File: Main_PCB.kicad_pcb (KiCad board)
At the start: 4 copper layers, 161 x 70 mm, 64 parts, among them IC1 TCN75AVUA713-VAO, IC2 24AA64T-I_OT, J1 Conn_Coaxial, J2 Conn_02x03_Odd_Even, J3 USB_C_Receptacle_USB2.0, J4 Conn_01x03_Male, SW1 SW_Push, SW2 SW_Push, U1 LTR-329ALS-01, U2 RFM95W-868S2, U3 1013, U4 STM32L476RGTx, U5 ATECC508A-SSHDA-T, U7 USBLC6-2SC6, Y1 32.768

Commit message: finished pcb
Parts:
- added ?: , logo's:PULU_LOGO_10MM, F.Cu at (178.5, 72.0)
- added J5: Conn_01x08, Connector_JST:JST_EH_B8B-EH-A_1x08_P2.50mm_Vertical, F.Cu at (100.2, 64.7)
- added J6: Conn_01x08, Connector_JST:JST_EH_S8B-EH_1x08_P2.50mm_Horizontal, B.Cu at (198.8, 80.5)
- added U6: ST-Nucleo-L432KC, Module:ST-Nucleo-L432KC, F.Cu at (136.0, 90.8)
- U5: value ATECC508A-SSHDA-T -> ATECC508A
- moved C6 74.0 mm to (73.2, 75.5), turned to 90 degrees
- moved IC1 73.9 mm to (70.8, 75.5), turned to 90 degrees
- moved D1 5.83 mm to (190.0, 72.2), turned to -90 degrees
- moved R10 4.42 mm to (190.0, 76.2), turned to -90 degrees
- moved C11 1.69 mm to (101.5, 70.5)
- moved C3 1.29 mm to (96.0, 70.5)
- moved C4 1.29 mm to (96.0, 72.5)
- moved Y1 1.29 mm to (99.0, 71.5)
- moved C8 0.92 mm to (117.5, 71.0)
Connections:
- net /D4 renamed /LED
- U4 pad 10: /PC2 -> unconnected-(U4-Pad10)
- U4 pad 11: /PC3 -> unconnected-(U4-Pad11)
- U4 pad 2: /PC13 -> unconnected-(U4-Pad2)
- U4 pad 24: /PC4 -> unconnected-(U4-Pad24)
- U4 pad 25: /PC5 -> unconnected-(U4-Pad25)
- U4 pad 26: /A3 -> unconnected-(U4-Pad26)
- U4 pad 27: /PB1 -> unconnected-(U4-Pad27)
- U4 pad 29: /D6 -> unconnected-(U4-Pad29)
- U4 pad 30: /PB11 -> unconnected-(U4-Pad30)
- U4 pad 33: /PB12 -> unconnected-(U4-Pad33)
- U4 pad 36: /PB15 -> unconnected-(U4-Pad36)
- U4 pad 37: /PC6 -> unconnected-(U4-Pad37)
- U4 pad 38: /D9 -> unconnected-(U4-Pad38)
- U4 pad 39: /PC8 -> unconnected-(U4-Pad39)
- U4 pad 40: /PC9 -> unconnected-(U4-Pad40)
- U4 pad 41: /D7 -> unconnected-(U4-Pad41)
- U4 pad 42: /D8 -> unconnected-(U4-Pad42)
- U4 pad 5: /PH0 -> unconnected-(U4-Pad5)
- U4 pad 51: /PC10 -> unconnected-(U4-Pad51)
- U4 pad 52: /PC11 -> unconnected-(U4-Pad52)
- U4 pad 53: /PC12 -> unconnected-(U4-Pad53)
- U4 pad 54: /PD2 -> unconnected-(U4-Pad54)
- U4 pad 56: /D5 -> unconnected-(U4-Pad56)
- U4 pad 58: /D10 -> unconnected-(U4-Pad58)
- U4 pad 59: /PB7 -> unconnected-(U4-Pad59)
- U4 pad 6: /PH1 -> unconnected-(U4-Pad6)
- U4 pad 61: /PB8 -> unconnected-(U4-Pad61)
- U4 pad 62: /PB9 -> unconnected-(U4-Pad62)
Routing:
- net /IC2_MoistureSensor_SCL1: track 177.8 -> 297.9 mm, vias 5 -> 8
- net /battery: track 94.0 -> 209.2 mm, vias 1 -> 3
- net /IC2_MoistureSensor_SDA1: track 192.6 -> 291.0 mm, vias 6 -> 10
- net /bat_voltage: track 21.1 -> 87.7 mm, vias 2 -> 7
- net VBAT: track 156.5 -> 218.6 mm, vias 2 -> 4
- net Lora-Reset: track 34.7 -> 91.4 mm, vias 0 -> 3
- net /LED: track 86.5 -> 138.2 mm, vias 0 -> 1
- net /SPI_LORA_SCK: track 47.8 -> 97.5 mm, vias 4 -> 6
- net /SPI_LORA_MISO: track 51.7 -> 99.0 mm, vias 4 -> 6
- net /SPI_LORA_NSS: track 36.5 -> 83.7 mm, vias 1 -> 3
- net /D1_TX: track 0.00 -> 34.8 mm, vias 0 -> 3
- net /Reset: track 89.4 -> 123.4 mm, vias 4 -> 6
- net /D0_TX: track 0.00 -> 32.0 mm, vias 0 -> 3
- net /SPI_LORA_MOSI: track 52.6 -> 80.3 mm, vias 4 -> 6
- net /boot0: track 100.0 -> 72.4 mm, vias 5 -> 2
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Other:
- outline, holes or cut-outs redrawn
- board text added: "+"
- board text added: "-"
- board text added: "2x 1A fast acting"
- board text added: "J-Link prog port"
- board text added: "Pulu soil monitor v1.0"

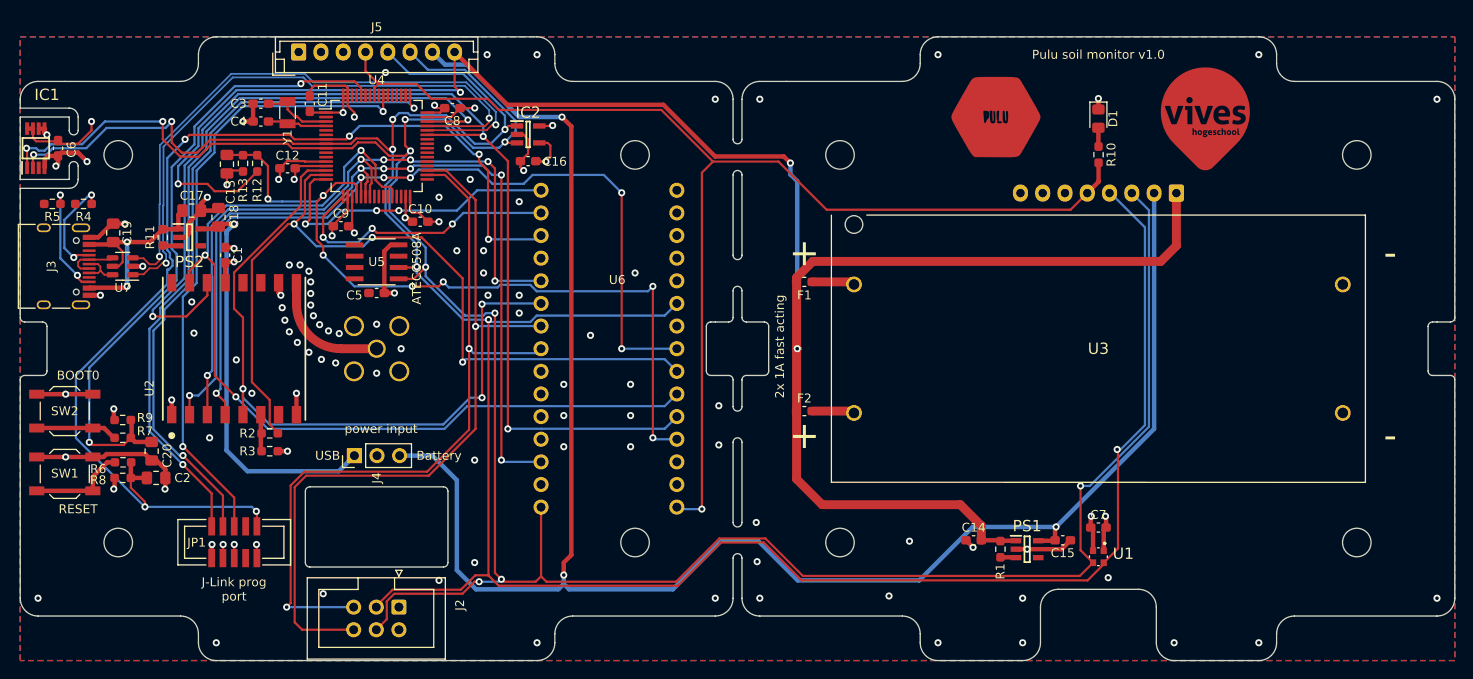
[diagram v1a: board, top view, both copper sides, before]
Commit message: updated b2b connector
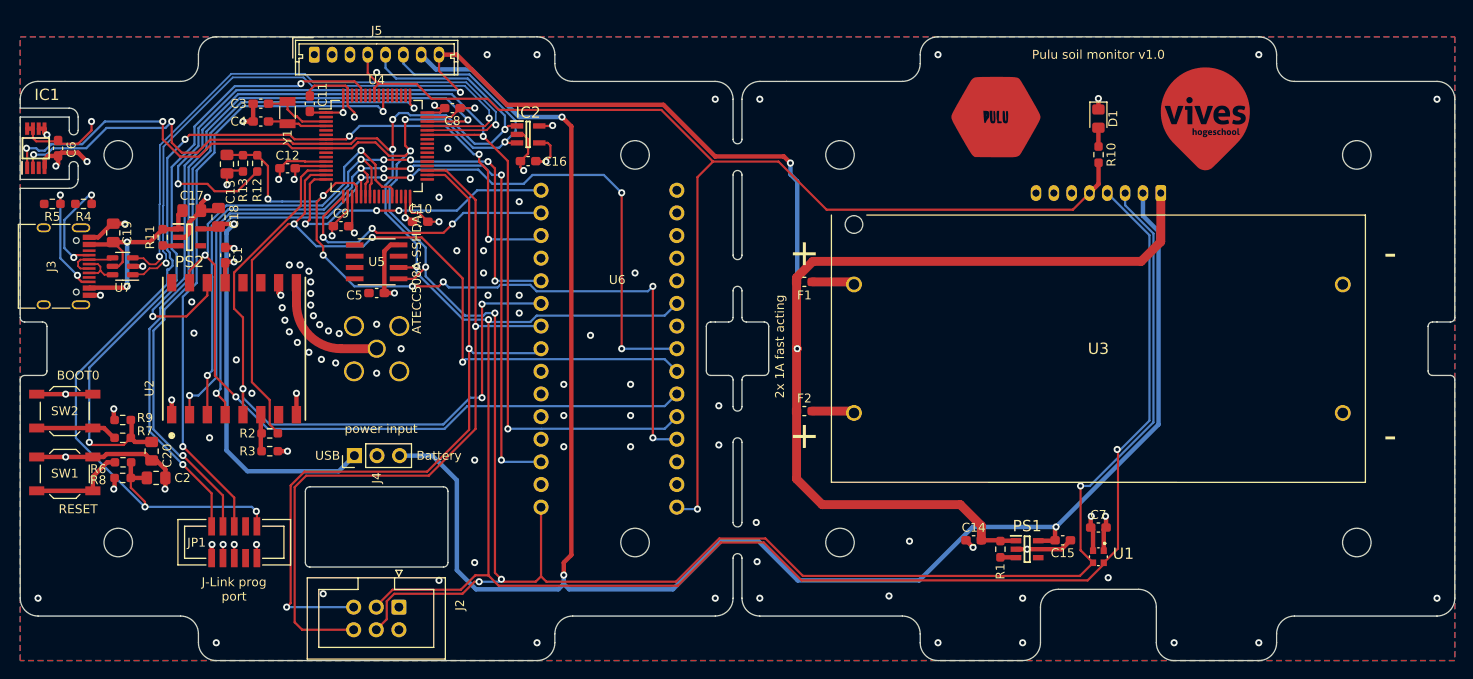
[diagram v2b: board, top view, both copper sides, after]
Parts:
- J5: footprint Connector_JST:JST_EH_B8B-EH-A_1x08_P2.50mm_Vertical -> Connector_Molex:Molex_Micro-Latch_53253-0870_1x08_P2.00mm_Vertical
- J6: footprint Connector_JST:JST_EH_S8B-EH_1x08_P2.50mm_Horizontal -> Connector_Molex:Molex_Micro-Latch_53253-0870_1x08_P2.00mm_Vertical
- U5: value ATECC508A -> ATECC508A-SSHDA-T
- moved J5 1.78 mm to (102.0, 65.0)
- moved J6 1.75 mm to (197.0, 80.5)
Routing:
- net /battery: track 209.2 -> 211.2 mm
- net /IC2_MoistureSensor_SDA1: track 291.0 -> 292.9 mm
- net /IC2_MoistureSensor_SCL1: track 297.9 -> 299.4 mm
- net /LED: track 138.2 -> 137.6 mm

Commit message: made drc complete
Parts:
- U5: value ATECC508A-SSHDA-T -> ATECC508A
- moved J3 0.11 mm to (72.8, 88.8)
- renumbered REF** to REF1, REF** to REF2, REF** to REF3, REF** to REF4, REF** to REF5, REF** to REF6, REF** to REF7, REF** to REF8
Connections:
- IC1 pad 3: unconnected-(IC1-Pad3) -> /TempAlert
- U4 pad 10: unconnected-(U4-Pad10) -> /TempAlert
- U6 pad 28: unconnected-(U6-Pad28) -> /Reset
- U6 pad 29: unconnected-(U6-Pad29) -> GND
- U6 pad 9: unconnected-(U6-Pad9) -> /TempAlert
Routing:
- net /TempAlert: track 0.00 -> 89.8 mm, vias 0 -> 5
- net /Reset: track 123.4 -> 139.0 mm
- net /IC2_MoistureSensor_SDA1: track 292.9 -> 289.6 mm
- net /SWO: track 70.1 -> 72.5 mm
- net /IC2_MoistureSensor_SCL1: track 299.4 -> 297.7 mm
- net /boot0: track 72.4 -> 73.0 mm
- net /LORA_DIO0: track 127.5 -> 128.0 mm

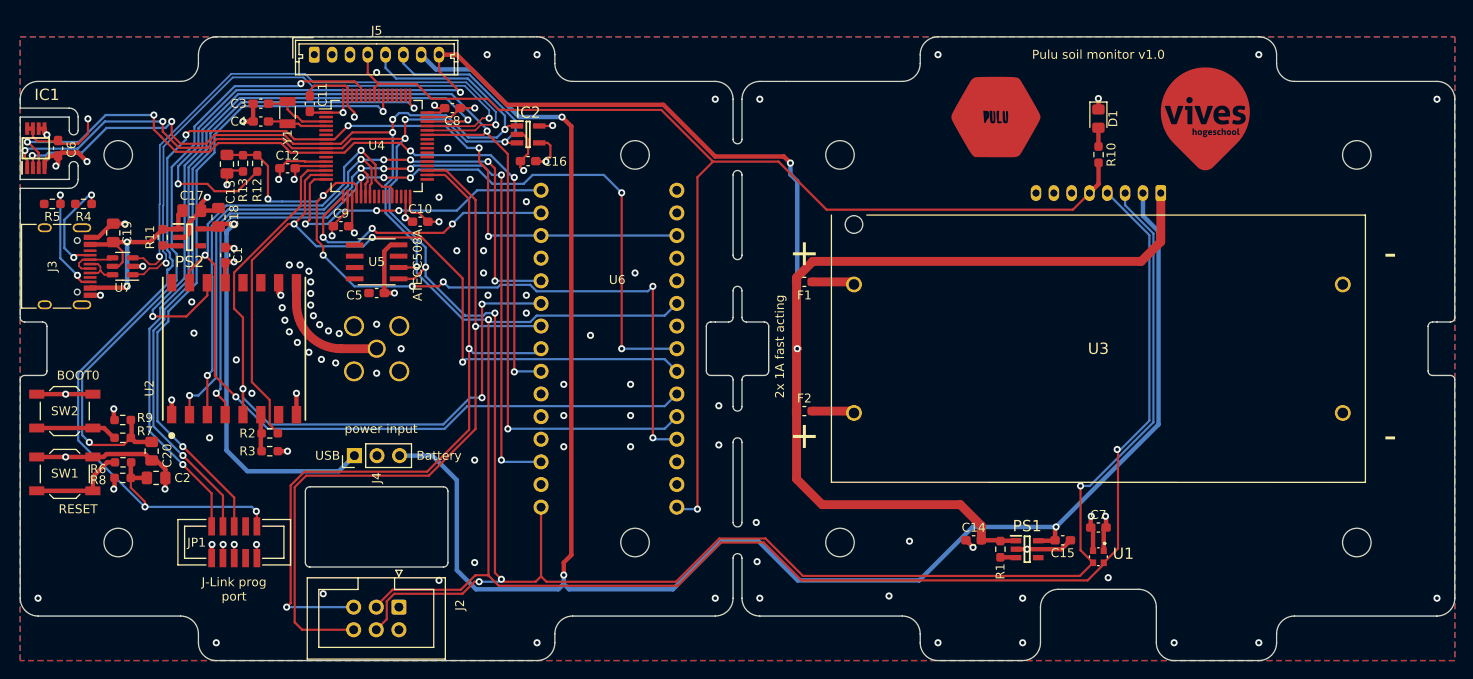
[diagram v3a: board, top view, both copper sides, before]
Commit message: updated eeprom footprint
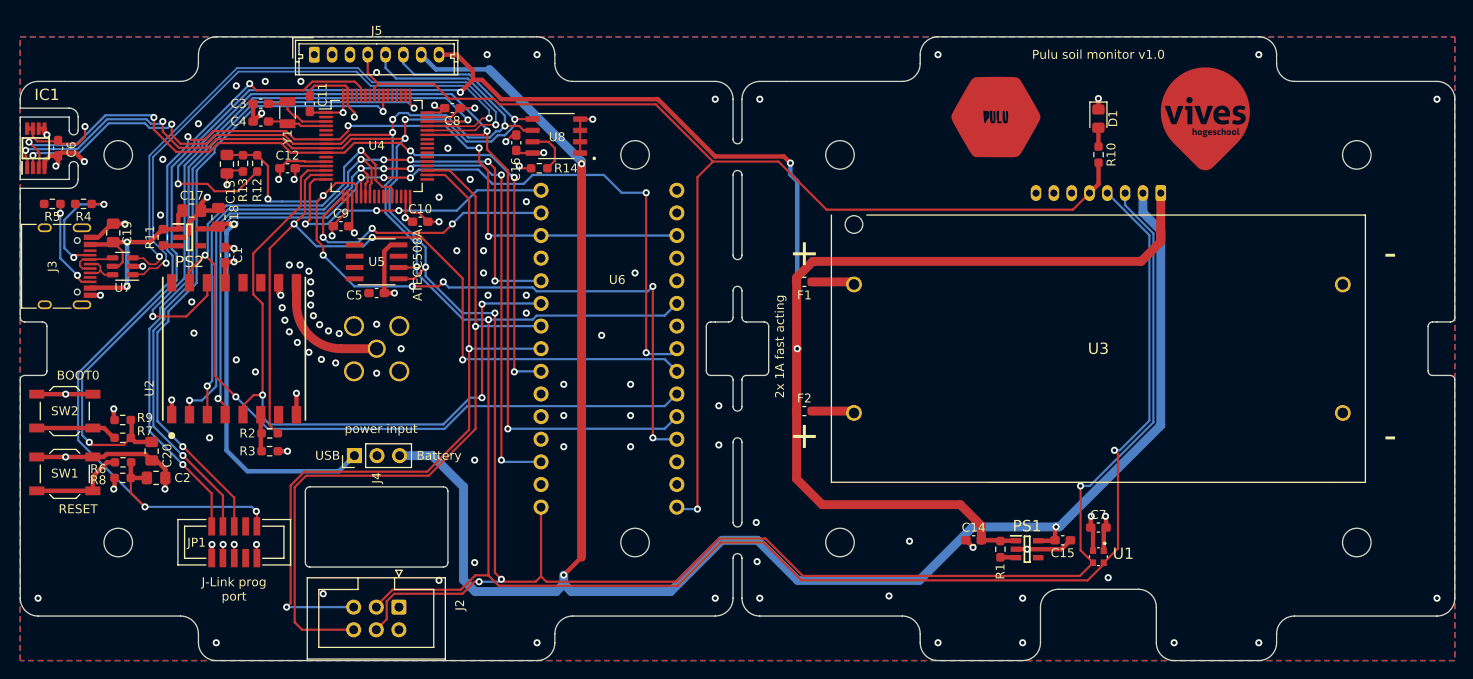
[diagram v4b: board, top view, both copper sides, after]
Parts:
- removed IC2: 24AA64T-I_OT, 24AA64T-I_OT:SOT95P270X145-5N
- added R14: 0R, Resistor_SMD:R_0603_1608Metric_Pad0.98x0.95mm_HandSolder, F.Cu at (127.2, 77.8)
- added U8: 24LC64-I/SN, 24LC64-I_SN:SOIC127P599X175-8N, F.Cu at (129.2, 74.1)
- moved C16 2.46 mm to (124.7, 74.9), turned to -90 degrees
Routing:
- net Net-(U8-Pad7): track 0.00 -> 5.40 mm
- net /SPI_LORA_NSS: track 83.7 -> 79.8 mm
- net VBAT: track 218.6 -> 215.1 mm
- net VCC: track 60.0 -> 56.5 mm
- net Lora-Reset: track 91.4 -> 89.1 mm
- net Net-(J3-PadB5): track 12.7 -> 10.7 mm
- net /IC2_MoistureSensor_SCL1: track 297.7 -> 299.3 mm
- net USB-: track 68.6 -> 70.1 mm
- net USB+: track 67.0 -> 68.5 mm
- net Net-(J3-PadA5): track 11.8 -> 13.2 mm
- net GND: track 119.7 -> 120.8 mm, vias 103 -> 110
- net /LORA_DIO0: track 128.0 -> 127.2 mm
- net /SWDIO: track 86.4 -> 85.6 mm
- net /SWO: track 72.5 -> 71.7 mm
- net /SWCLK: track 76.2 -> 75.4 mm
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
